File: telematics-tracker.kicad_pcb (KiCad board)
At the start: 4 copper layers, 80 x 60 mm, 223 parts, among them J1 WAFER-MX3.0-12PZZ, J2 B3B-XH-A, Q1 AM2390N-TP, Q10 MMBT3904, Q11 MMBT3904, Q12 MMBT3904, Q13 MMBT3906, Q14 MMBT3904, Q2 AM2390N-TP, Q3 AO3401A, Q4 MMBT3904, Q5 MMBT3904, Q6 MMBT3904, Q7 MMBT3904, Q8 MMBT3904, Q9 MMBT3904, U1 EC200UCNAA-N05-SGNSA, U2 AT32F403ACGT7, U3 QMI8658B, U4 SIT1051AT/3, U5 EG11752, U6 BQ25606RGER, U7 GD25Q64ESIGR, U8 TXB0104PWR, U9 ME6211C33M5G, X1 NANO-SIM, X2 MFF2-eSIM-pads, Y1 8MHz, Y2 32.768kHz

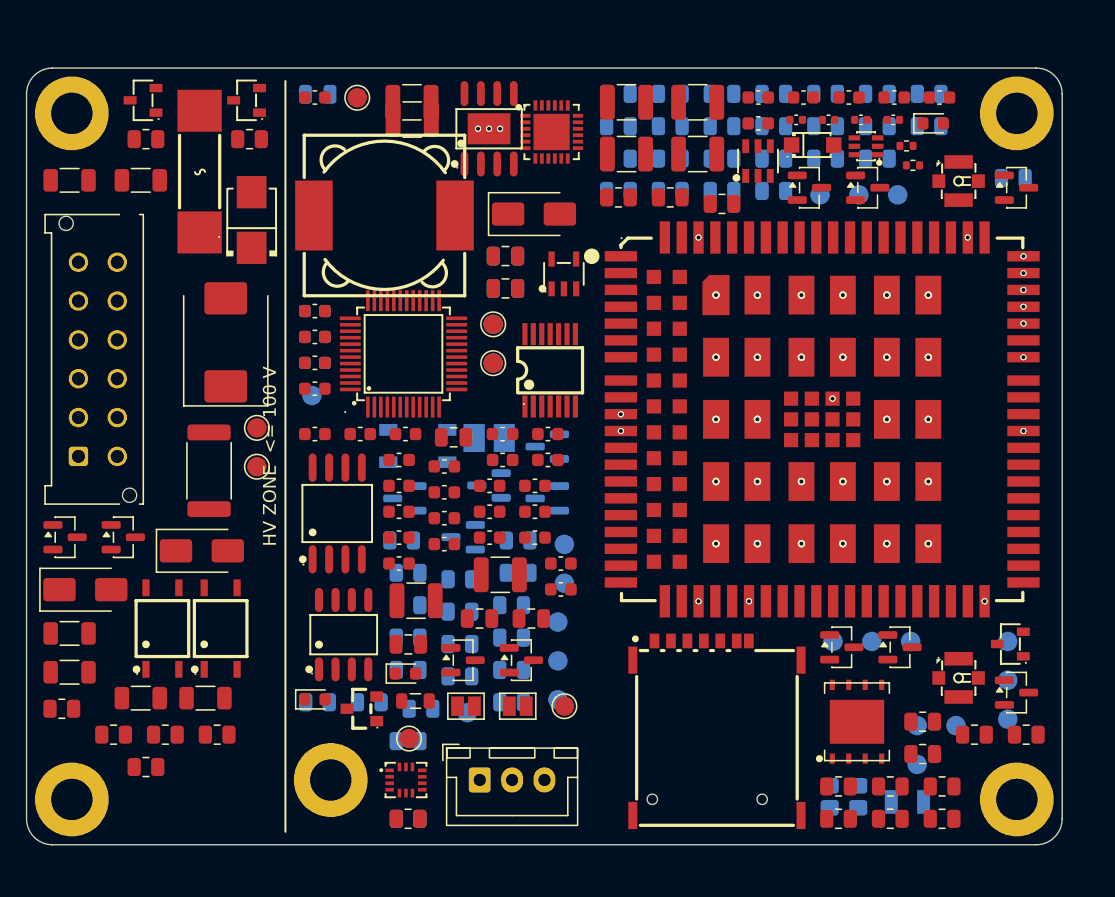
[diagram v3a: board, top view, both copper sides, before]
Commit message: F-20 confirmed as safety-critical; buck cluster courtyard overlaps 3 -> 0
F-20 CONFIRMED: conformal coating is a safety-critical PROCESS requirement,
not a finish preference - creepage at U5 depends on it. Uncoated at 100 V
needs 0.60 mm (IPC-2221 B1) and the EG11752 package gives 0.55 mm; coated (B4)
needs ~0.25 mm. Recorded in four places so it cannot be lost: SKILL.md P1,
handoff section 6.1 + rule 6, the .kicad_dru exception (now explicitly valid
ONLY while coating is mandatory), and the installation sheet. Prototypes are
coated before the 100 V / 85 C burn-in. U5 is marked on F.Fab with a boxed
outline and "COATING INSPECTION - CREEPAGE CRITICAL (F-20)". The 0.3 mm
exception stays scoped to HV_ZONE.

BUCK CLUSTER: courtyard overlaps 3 -> 0, and the inductor was NOT the cause.
Measured all three options rather than assuming:
  grow board to 82/84/86 mm  -> 2 / 2 / 2  (plateaus, never reaches 0)
  synthetic 10x10 inductor   -> 1          (better, still not 0)
  restructure into a column  -> 0
Root cause was C73/C74 stacked in the 4.2 mm strip ABOVE L1, needing 3.29 mm
each; C73 was clamped on the zone edge and L1 blocked C74, so the relaxation
converged them to 3.08 mm apart regardless of anchoring. Fixed by making the
cluster a column beside L1 ordered to follow the hot loop (D16 above U5 since
SW is pin 6 on the upper edge, C73 below since VIN is pin 8 on the lower),
moving U6 next to J2 where it belongs electrically, and un-anchoring U9 and
C74 (only the cap nearest U5's VIN pin is loop-critical).

INDUCTOR: researched and logged as instructed, but NOT applied. C5142144
(YNR1050-151M, 150uH, Isat 2.0A, 10x10x5, 496 stock, $0.162) qualifies, but
the area saving is no longer needed and the swap costs DCR +56% (280 -> 438
mOhm, i.e. 0.280 -> 0.438 W at 1.0 A, ~3.2% of the 5 W output), Irms 1.42 ->
1.20 A, Isat 2.70 -> 2.00 A on differing criteria (25% vs 30% drop), stock
5132 -> 496, a new footprint, and unverified core loss. Incumbent C21325 is
retained; C514214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
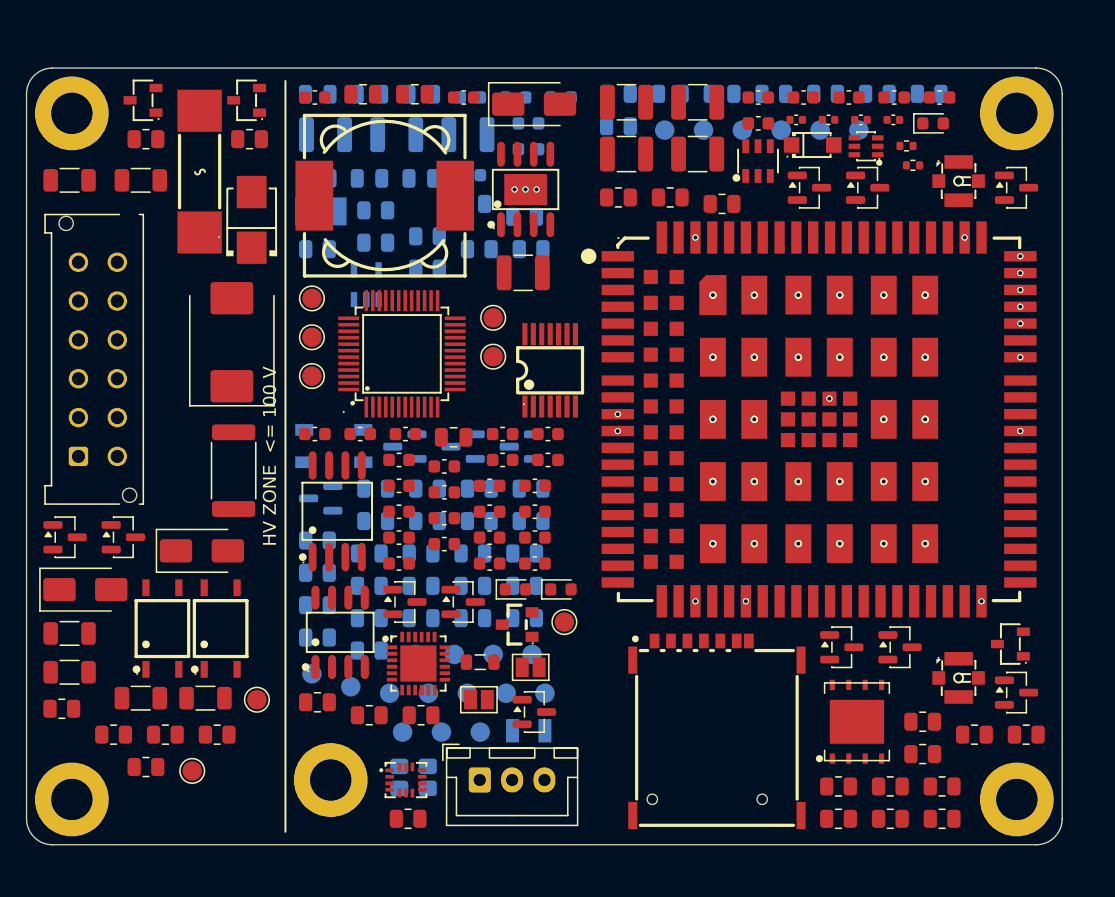
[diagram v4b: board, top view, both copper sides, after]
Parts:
- C68, C69, C70, C71, C72, C74, C77, C78, C79, R46, R47, R48, R49, R5, TP10, U9: moved to B.Cu
- Q4, R11, R12, R2, R58, R59, R60, R61, R62, TP22, TP23: moved to F.Cu
- moved R7 61.6 mm to (22.5, 44.0)
- moved R59 57.5 mm to (70.7, 55.5), turned to 0 degrees
- moved R58 57.5 mm to (66.7, 55.5), turned to 0 degrees
- moved R62 56.2 mm to (70.7, 58.0), turned to 0 degrees
- moved R60 56.2 mm to (62.7, 58.0), turned to 0 degrees
- moved R61 56.2 mm to (66.7, 58.0), turned to 0 degrees
- moved R50 52.1 mm to (45.7, 9.99)
- moved R85 49.5 mm to (27.0, 13.5)
- moved R51 47.2 mm to (49.7, 9.99)
- moved R52 45.9 mm to (53.7, 10.5)
- moved R8 44.5 mm to (26.5, 45.0)
- moved R6 43.3 mm to (38.5, 42.5)
- moved U6 42.3 mm to (30.3, 46.0)
- moved R48 42.0 mm to (26.5, 42.5), turned to 180 degrees
- moved TP28 41.9 mm to (34.0, 48.3)
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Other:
- board text added: "COATING INSPECTION - CREEPAGE CRITICAL (F-20)"

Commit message: Checks 1/3/4/5/7 now pass: RF corridor, HV spacing, VBAT caps. 7 of 8.
CHECK 1 PASS. U1 moved inboard and down (x 61->59->61 after the X growth,
y 27->29) to open a two-sided fenced CPWG corridor:
  ANT pad outer edge x=77.80, board edge x=82.05 -> usable strip 3.95 mm
  requirement 3.10 mm (W 0.40 + 2xG 0.30 + 2x(2W standoff + via radius))
  ANT_MAIN U1.49 -> AF1.3 = 13.40 mm, ANT_GNSS U1.47 -> AF2.3 = 20.35 mm
R71/R72 anchored inline, 0.88 mm pad-to-pad from their ANT pad (<= 2 mm) and
outboard of it. Q3 moved off the RF edge to beside the VBAT caps. Both dog-leg
corridors clear of non-GND pads and vias.

OUTLINE GREW TWICE, both forced, both logged in tools/pcbgen.py:
  Y 60 -> 62: AF1 must clear H2's 6.29 mm M3 pad (reaching y=6.65) so U1 y >=
    28.15, while X1 (15.09 mm tall) must fit below U1 so U1 y <= 27.51 -
    infeasible by 0.64 mm.
  X 80 -> 82: moving U1 inboard took 2 mm off the power zone, leaving the buck
    cluster single-file in a 5.35 mm strip and putting C73's VIN_B pad 0.215 mm
    from U5's LV pins. Growing X back and returning U1 to x=61 keeps the
    3.95 mm corridor AND restores the 22.25 mm power zone.
Still provisional - final outline comes from the purchased housing.

CHECK 3 PASS. Split permanently into intra- and inter-component metrics.
Intra-component pairs are exempt at <= 40 V, with the voltages computed from
the divider: 3x100k then 9.1k = 309.1k, so at VIN=100 V I=323.5 uA and each
100k drops 32.35 V (EXEMPT). Above 40 V and listed separately: Q1/Q2 at 100 V
(LV gate against HV drain, 1.04 mm), R40 at 91.66 V, the DI series resistors,
and the optos - these rely on the IPC-2221 figure for their actual voltage plus
the mandatory coating, same basis as F-20. Flagged: R40 is the DNP spare and is
a SINGLE 100k, so it sees 91.7 V where the fitted dividers see 32.35 V; it
should be 3x100k if ever populated.
Between-component minimum is now 1.779 mm (was 1.025 mm).

The packer enforces this with PER-PAD semantics. Classifying a part si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
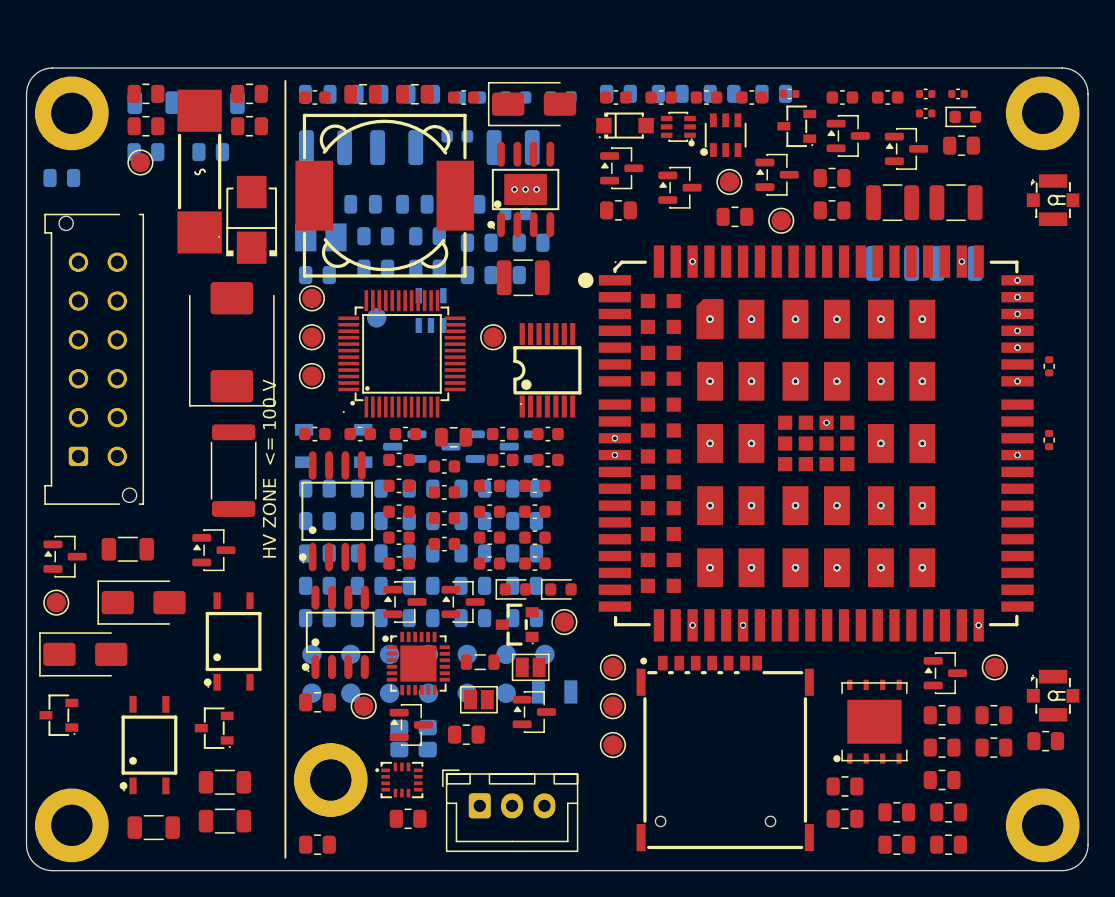
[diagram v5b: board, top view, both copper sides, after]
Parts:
- C81, C82, R18, R19, R32, R35, R40, TP23: moved to B.Cu
- Q5, R63, R64, R65, R66, TP10, TP14, TP15, TP16, TP17, TP18, TP24: moved to F.Cu
- moved R63 61.1 mm to (71.2, 57.5), turned to 0 degrees
- moved R65 59.6 mm to (67.2, 60.0), turned to 0 degrees
- moved R66 59.6 mm to (71.2, 60.0), turned to 0 degrees
- moved R64 57.6 mm to (63.2, 58.0), turned to 0 degrees
- moved TP24 51.2 mm to (45.3, 52.3), turned to 0 degrees
- moved Q2 48.6 mm to (14.5, 51.0)
- moved Q1 47.9 mm to (2.50, 50.0)
- moved R34 47.4 mm to (17.2, 4.50)
- moved TP18 47.3 mm to (45.3, 49.3), turned to 0 degrees
- moved R33 47.1 mm to (9.22, 4.50)
- moved R15 47.0 mm to (15.3, 55.2)
- moved R18 46.0 mm to (9.82, 2.67), turned to 180 degrees
- moved R19 46.0 mm to (14.8, 2.67), turned to 180 degrees
- moved R40 46.0 mm to (2.73, 8.49), turned to 180 degrees
- moved R35 45.0 mm to (14.2, 6.50), turned to 180 degrees
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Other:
- board size 80 x 60 mm -> 82 x 62 mm

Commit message: GNSS bias-T (DNP) per Quectel fig 31; check 2 reclassified; log 7-of-8
ANT_GNSS pin 47 is AI, 50 ohm, with NO internal DC feed (Table 37 p.67), so an
external bias-T is correct. Quectel figure 31 (p.68) is itself the reference
bias-T and its values are what the schematic now uses: L4 47nH series, C84
100pF shunt, R90 10R + C83 100nF on the 3V3 feed, all DNP - note 2 says the
VDD circuit is not needed for a passive antenna.

NEW FLAG F-21: Quectel's figure DC-couples the module pin to the injection node
through the 0R, so 3V3 would sit on ANT_GNSS with the bias-T fitted. The R72
position is documented 0R-or-DC-block. Do not populate until settled.

Check 2 reclassified as instructed: PCB copper keepout is N/A because both
antennas are lid-mounted and reach the board only by U.FL pigtail; the
metal-clearance figure becomes an installation/housing requirement. Still FAIL
pending antenna selection. Fixed a checker false positive - R80's value
'1R 2512 anti-surge' contains the substring ANT.

ERC 0/13, checkpins exit 0, DRC 19 + 452 unconnected.

Co-Authored-By: Claude Opus 5 (1M context) <noreply@anthropic.com>
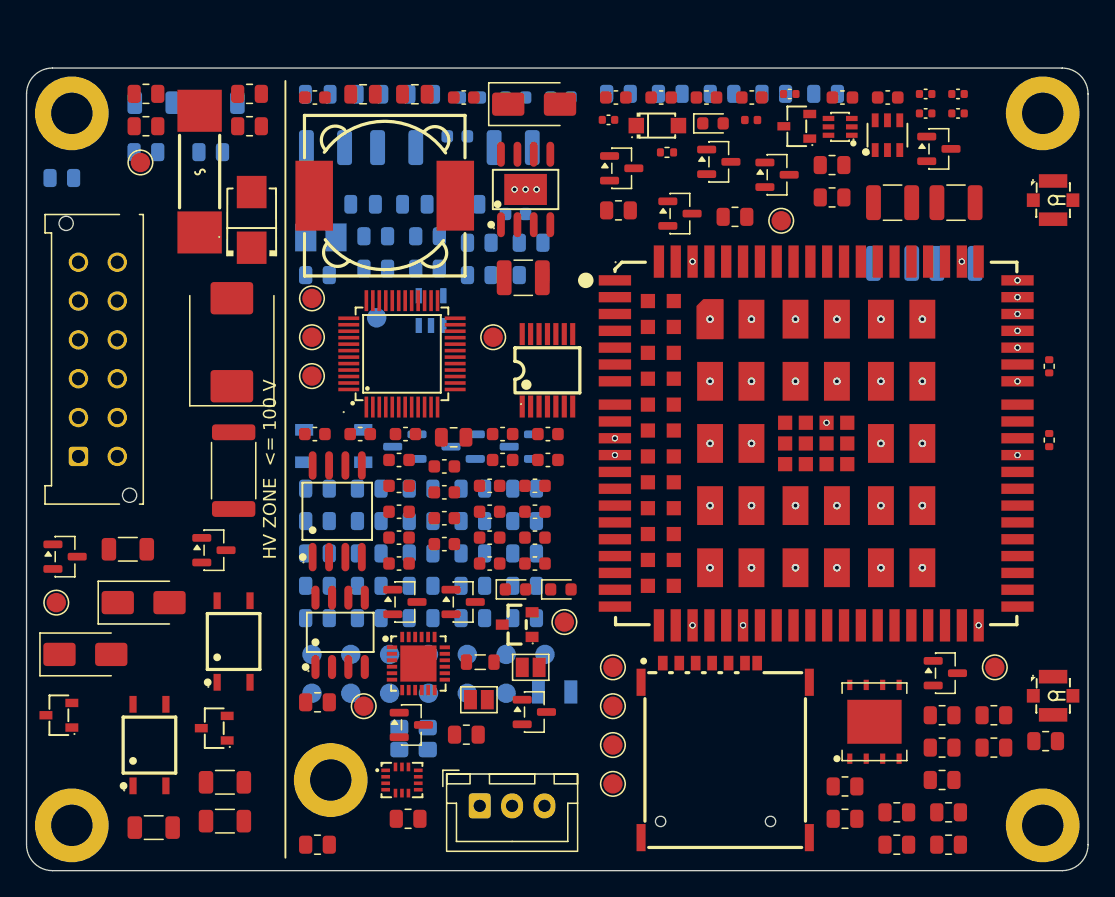
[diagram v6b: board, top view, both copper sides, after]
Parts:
- removed the D14 at (50.4, 4.54)
- removed the J2 at (35.0, 57.0)
- removed the L1 at (27.7, 9.86)
- removed the L3 at (22.7, 13.1)
- added C9: 100nF, C_0603_1608Metric, F.Cu at (39.3, 38.3)
- added D1: S3M, SMB_L4.3-W3.6-LS5.3-RD, F.Cu at (17.4, 11.7)
- added D15: USBLC6-2SC6, SOT-23-6_L2.9-W1.6-P0.95-LS2.8-BL, F.Cu at (66.5, 5.19)
- added JP1: BOOT0_SEL, SolderJumper-2_P1.3mm_Open_Pad1.0x1.5mm, F.Cu at (38.9, 46.3)
- added L2: ACT45B-510-2P, IND-SMD_4P-L4.5-W3.2-TL, B.Cu at (23.7, 29.2)
- added L4: 47nH DNP, L_0402_1005Metric, F.Cu at (56.0, 4.01)
- added OK1: EL357N(D), OPTO-SMD-4_L4.4-W4.1-P2.54-LS7.0-BL, F.Cu at (16.0, 44.3)
- added R90: 10R DNP, R_0402_1005Metric, F.Cu at (49.5, 6.51)
- C83: renamed from C9; value 100nF -> 100nF DNP; footprint C_0603_1608Metric -> C_0402_1005Metric
- C84: renamed from D1; value S3M -> 100pF DNP; footprint SMB_L4.3-W3.6-LS5.3-RD -> C_0402_1005Metric
- D14: renamed from D15; value USBLC6-2SC6 -> SMF05C; footprint SOT-23-6_L2.9-W1.6-P0.95-LS2.8-BL -> SOT-363_L2.0-W1.3-P0.65-LS2.1-BR
- J2: renamed from JP1; value BOOT0_SEL -> B3B-XH-A; footprint SolderJumper-2_P1.3mm_Open_Pad1.0x1.5mm -> JST_XH_B3B-XH-A_1x03_P2.50mm_Vertical
- L1: renamed from L2; value ACT45B-510-2P -> 150uH 2.7A; footprint IND-SMD_4P-L4.5-W3.2-TL -> IND-SMD_L12.3-W12.3; moved to F.Cu
- L3: renamed from OK1; value EL357N(D) -> 2.2uH; footprint OPTO-SMD-4_L4.4-W4.1-P2.54-LS7.0-BL -> L1008; moved to B.Cu
- R66: moved to B.Cu
- moved R66 63.4 mm to (45.7, 2.00), turned to 180 degrees
- moved C83 47.7 mm to (72.0, 3.50)
- moved R54 41.7 mm to (70.7, 50.0)
- moved TP15 36.9 mm to (45.3, 46.3)
- moved L3 31.9 mm to (22.7, 13.1), turned to 180 degrees
- moved TP17 29.7 mm to (45.3, 49.3)
- moved TP16 29.5 mm to (74.8, 46.3)
- moved C84 28.6 mm to (45.0, 4.00), turned to 0 degrees
- moved L1 19.7 mm to (27.7, 9.86), turned to 0 degrees
- moved D13 19.5 mm to (53.0, 4.28)
- moved Q11 14.5 mm to (53.5, 7.25)
- moved J2 11.4 mm to (35.0, 57.0)
- moved R50 10.1 mm to (62.2, 7.50)
- moved D14 8.87 mm to (62.9, 4.54)
- moved R57 8.02 mm to (70.7, 52.5)
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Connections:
- C83 pad 1: 3V3 -> /modem_rf/GNSS_BIAS
- C84 pad 1: /power/VIN_P -> /modem_rf/ANT_GNSS_C
- C84 pad 2: /power/VIN_F -> GND
- D14 pad 1: /modem_rf/USB_DP_M -> /modem_rf/SIM_DATA
- D14 pad 3: /modem_rf/USB_DM_M -> /modem_rf/SIM_CLK
- D14 pad 4: /modem_rf/USB_DM_TP -> /modem_rf/SIM_RST
- D14 pad 5: /modem_rf/USB_VBUS -> /modem_rf/USIM_VDD
- D14 pad 6: /modem_rf/USB_DP_TP -> (no net)
- J2 pad 1: 3V3 -> /power/VBAT_BT
- J2 pad 2: /mcu/BOOT0 -> /power/U6_TS
- L1 pad 1: /io/CANH -> /power/SW_BUCK
- L1 pad 2: /io/CANL -> 5V0
- L3 pad 1: /io/DI1_LED -> /power/SW_CHG
- L3 pad 2: GND -> SYS
